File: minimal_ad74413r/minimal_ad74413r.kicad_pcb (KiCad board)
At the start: 4 copper layers, 30.5 x 25.4 mm, 17 parts, among them U8 AD74413RBCPZ

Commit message: backup
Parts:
- added C1: 0.01 uF, capacitor_footprints:C_0402_1005Metric, F.Cu at (161.6, 105.2)
- added C10: 0.01 uF, capacitor_footprints:C_0402_1005Metric, F.Cu at (141.9, 97.0)
- added C11: 220 pF, capacitor_footprints:C_0402_1005Metric, F.Cu at (138.7, 99.2)
- added C12: 0.01 uF, capacitor_footprints:C_0402_1005Metric, F.Cu at (137.9, 97.4)
- added C13: 0.01 uF, capacitor_footprints:C_0402_1005Metric, F.Cu at (141.9, 105.2)
- added C14: 0.01 uF, capacitor_footprints:C_0402_1005Metric, F.Cu at (141.9, 108.5)
- added C15: 220 pF, capacitor_footprints:C_0402_1005Metric, F.Cu at (138.7, 106.3)
- added C16: 0.01 uF, capacitor_footprints:C_0402_1005Metric, F.Cu at (137.9, 108.1)
- added C2: 0.01 uF, capacitor_footprints:C_0402_1005Metric, F.Cu at (161.6, 108.5)
- added C3: 220 pF, capacitor_footprints:C_0402_1005Metric, F.Cu at (164.9, 106.3)
- added C4: 0.01 uF, capacitor_footprints:C_0402_1005Metric, F.Cu at (165.7, 108.1)
- added C5: 0.01 uF, capacitor_footprints:C_0402_1005Metric, F.Cu at (161.6, 100.3)
- added C6: 0.01 uF, capacitor_footprints:C_0402_1005Metric, F.Cu at (161.6, 97.0)
- added C7: 220 pF, capacitor_footprints:C_0402_1005Metric, F.Cu at (164.9, 99.2)
- added C8: 0.01 uF, capacitor_footprints:C_0402_1005Metric, F.Cu at (165.7, 97.4)
- added C9: 0.01 uF, capacitor_footprints:C_0402_1005Metric, F.Cu at (141.9, 100.3)
- added CR1: SBAV99WT1G, diode_footprints:SC_70, F.Cu at (162.4, 112.7)
- added CR2: SBAV99WT1G, diode_footprints:SC_70, F.Cu at (162.4, 92.8)
- added CR3: SBAV99WT1G, diode_footprints:SC_70, F.Cu at (141.1, 92.8)
- added CR4: SBAV99WT1G, diode_footprints:SC_70, F.Cu at (141.1, 112.7)
- added Q1: ZXMP6A17E6TA, transistor_footprints:SOT-26, F.Cu at (159.0, 112.0)
- added Q2: ZXMP6A17E6TA, transistor_footprints:SOT-26, F.Cu at (159.0, 93.5)
- added Q3: ZXMP6A17E6TA, transistor_footprints:SOT-26, F.Cu at (144.5, 93.5)
- added Q4: ZXMP6A17E6TA, transistor_footprints:SOT-26, F.Cu at (144.5, 112.0)
- added R1: 2k, resistor_footprints:R_0402_1005Metric, F.Cu at (161.6, 110.8)
- added R10: 100, resistor_footprints:R_0805_2012Metric, F.Cu at (164.1, 97.0)
- added R11: 2k, resistor_footprints:R_0402_1005Metric, F.Cu at (141.9, 94.7)
- added R12: 10k, resistor_footprints:R_0402_1005Metric, F.Cu at (141.9, 95.9)
- added R13: 2k, resistor_footprints:R_0402_1005Metric, F.Cu at (141.9, 98.1)
- added R14: 10k, resistor_footprints:R_0402_1005Metric, F.Cu at (141.9, 99.2)
- added R15: 100, resistor_footprints:R_0805_2012Metric, F.Cu at (139.5, 97.0)
- added R16: 2k, resistor_footprints:R_0402_1005Metric, F.Cu at (141.9, 110.8)
- added R17: 10k, resistor_footprints:R_0402_1005Metric, F.Cu at (141.9, 109.6)
- added R18: 2k, resistor_footprints:R_0402_1005Metric, F.Cu at (141.9, 107.4)
- added R19: 10k, resistor_footprints:R_0402_1005Metric, F.Cu at (141.9, 106.3)
- added R2: 10k, resistor_footprints:R_0402_1005Metric, F.Cu at (161.6, 109.6)
- added R20: 100, resistor_footprints:R_0805_2012Metric, F.Cu at (139.5, 108.5)
- added R3: 2k, resistor_footprints:R_0402_1005Metric, F.Cu at (161.6, 107.4)
- added R4: 10k, resistor_footprints:R_0402_1005Metric, F.Cu at (161.6, 106.3)
- added R5: 100, resistor_footprints:R_0805_2012Metric, F.Cu at (164.1, 108.5)
- added R6: 2k, resistor_footprints:R_0402_1005Metric, F.Cu at (161.6, 94.7)
- added R7: 10k, resistor_footprints:R_0402_1005Metric, F.Cu at (161.6, 95.9)
- added R8: 2k, resistor_footprints:R_0402_1005Metric, F.Cu at (161.6, 98.1)
- added R9: 10k, resistor_footprints:R_0402_1005Metric, F.Cu at (161.6, 99.2)
- added TP1: TestPoint, test_point_footprints:TestPoint_THTPad_Castelated, F.Cu at (157.5, 118.7)
- added TP10: TestPoint, test_point_footprints:TestPoint_THTPad_Castelated, F.Cu at (149.9, 118.7)
- added TP11: TestPoint, test_point_footprints:TestPoint_THTPad_Castelated, F.Cu at (167.6, 113.7)
- added TP12: TestPoint, test_point_footprints:TestPoint_THTPad_Castelated, F.Cu at (167.6, 92.1)
- added TP13: TestPoint, test_point_footprints:TestPoint_THTPad_Castelated, F.Cu at (135.9, 92.1)
- added TP14: TestPoint, test_point_footprints:TestPoint_THTPad_Castelated, F.Cu at (135.9, 113.7)
- added TP15: TestPoint, test_point_footprints:TestPoint_THTPad_Castelated, F.Cu at (166.4, 113.7)
- added TP16: TestPoint, test_point_footprints:TestPoint_THTPad_Castelated, F.Cu at (166.4, 92.1)
- added TP17: TestPoint, test_point_footprints:TestPoint_THTPad_Castelated, F.Cu at (137.2, 92.1)
- added TP18: TestPoint, test_point_footprints:TestPoint_THTPad_Castelated, F.Cu at (137.2, 113.7)
- added TP19: TestPoint, test_point_footprints:TestPoint_THTPad_Castelated, F.Cu at (154.9, 87.0)
- added TP2: TestPoint, test_point_footprints:TestPoint_THTPad_Castelated, F.Cu at (156.2, 118.7)
- added TP20: TestPoint, test_point_footprints:TestPoint_THTPad_Castelated, F.Cu at (153.7, 87.0)
- added TP21: TestPoint, test_point_footprints:TestPoint_THTPad_Castelated, F.Cu at (152.4, 87.0)
- added TP22: TestPoint, test_point_footprints:TestPoint_THTPad_Castelated, F.Cu at (151.1, 87.0)
- added TP23: TestPoint, test_point_footprints:TestPoint_THTPad_Castelated, F.Cu at (149.9, 87.0)
- added TP24: TestPoint, test_point_footprints:TestPoint_THTPad_Castelated, F.Cu at (148.6, 87.0)
- added TP3: TestPoint, test_point_footprints:TestPoint_THTPad_Castelated, F.Cu at (154.9, 118.7)
- added TP4: TestPoint, test_point_footprints:TestPoint_THTPad_Castelated, F.Cu at (153.7, 118.7)
- added TP5: TestPoint, test_point_footprints:TestPoint_THTPad_Castelated, F.Cu at (152.4, 118.7)
- added TP6: TestPoint, test_point_footprints:TestPoint_THTPad_Castelated, F.Cu at (148.6, 118.7)
- added TP7: TestPoint, test_point_footprints:TestPoint_THTPad_Castelated, F.Cu at (147.3, 118.7)
- added TP8: TestPoint, test_point_footprints:TestPoint_THTPad_Castelated, F.Cu at (146.1, 118.7)
- added TP9: TestPoint, test_point_footprints:TestPoint_THTPad_Castelated, F.Cu at (151.1, 118.7)
- C82: footprint footprints:C_0603_1608Metric -> capacitor_footprints:C_0603_1608Metric
- moved C89 4.29 mm to (155.2, 92.5), turned to 90 degrees
- moved C91 2.89 mm to (149.9, 112.4), turned to 180 degrees
- moved C83 2.36 mm to (152.1, 112.4), turned to 0 degrees
- moved C93 2.22 mm to (142.3, 103.6)
- moved C84 2.06 mm to (152.1, 111.1), turned to 0 degrees
- moved C92 1.98 mm to (138.6, 102.9)
- moved U8 1.65 mm to (151.8, 102.9)
- moved C81 1.65 mm to (149.0, 96.6)
- moved C82 1.65 mm to (151.5, 95.7)
- moved C87 1.65 mm to (159.8, 102.6)
- moved C90 1.50 mm to (153.0, 93.5), turned to 90 degrees
- moved C95 1.46 mm to (165.0, 102.9)
- moved C86 1.43 mm to (162.1, 101.7)
- moved C94 1.43 mm to (162.1, 103.6)
- moved C85 1.43 mm to (163.2, 101.7)
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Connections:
- C88 pad 1: (no net) -> /3V3
- C89 pad 1: /3V3_ISO -> /3V3
- C90 pad 1: /3V3_ISO -> /3V3
- C91 pad 1: (no net) -> /3V3
- U8 pad 23: /3V3_ISO -> /3V3
- U8 pad 28: (no net) -> GNDA
- U8 pad 55: (no net) -> /3V3
- U8 pad 56: (no net) -> /3V3
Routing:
- net /3V3_ISO: track 16.6 -> 0.00 mm, vias 4 -> 0
- net /CCOMP_B: track 0.00 -> 15.7 mm, vias 0 -> 2
- net /CCOMP_C: track 0.00 -> 15.7 mm, vias 0 -> 2
- net /CCOMP_A: track 0.00 -> 15.6 mm, vias 0 -> 2
- net /CCOMP_D: track 0.00 -> 15.5 mm, vias 0 -> 2
- net /VIOUTP_C: track 0.00 -> 11.0 mm, vias 0 -> 2
- net /VIOUTP_A: track 0.00 -> 10.9 mm, vias 0 -> 2
- net /SDO: track 0.00 -> 9.13 mm
- net /~{RESET}: track 0.00 -> 9.13 mm
- net /~{ALERT}: track 0.00 -> 9.01 mm
- net /3V3: track 0.00 -> 8.95 mm, vias 0 -> 4
- net /~{LDAC}: track 0.00 -> 8.89 mm
- net /~{ADC_RDY}: track 0.00 -> 8.81 mm
- net /~{SYNC}: track 0.00 -> 8.81 mm
- net /SCLK: track 0.00 -> 8.71 mm
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- added copper zone on F.Cu, net /3V3
- added copper zone on In1.Cu, net /VDD_24V
- added copper zone on In1.Cu, net GNDA
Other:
- board size 30.5 x 25.4 mm -> 34.3 x 31.8 mm

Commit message: backup
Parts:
- added TP25: TestPoint, test_point_footprints:TestPoint_THTPad_Castelated, F.Cu at (133.3, 102.2)
- added TP26: TestPoint, test_point_footprints:TestPoint_THTPad_Castelated, F.Cu at (170.2, 102.2)
- moved TP23 26.2 mm to (170.2, 103.5), turned to 180 degrees
- moved TP24 22.5 mm to (133.3, 103.5), turned to 0 degrees
- moved TP19 1.80 mm to (153.7, 85.7)
- moved TP20 1.80 mm to (152.4, 85.7)
- moved TP22 1.80 mm to (149.9, 85.7)
- moved TP21 1.80 mm to (151.1, 85.7)
- moved C89 1.50 mm to (153.7, 92.4), turned to 180 degrees
- moved C96 1.48 mm to (148.5, 92.4), turned to 180 degrees
- moved TP1 1.27 mm to (157.5, 120.0)
- moved TP10 1.27 mm to (149.9, 120.0)
- moved TP2 1.27 mm to (156.2, 120.0)
- moved TP3 1.27 mm to (154.9, 120.0)
- moved TP4 1.27 mm to (153.7, 120.0)
- moved TP5 1.27 mm to (152.4, 120.0)
- moved TP6 1.27 mm to (148.6, 120.0)
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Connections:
- TP23 pad 1: /3V3 -> /VDD_24V
- TP24 pad 1: GNDA -> /VDD_24V
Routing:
- net /3V3: track 8.95 -> 0.00 mm, vias 4 -> 5
- net /~{ADC_RDY}: track 8.81 -> 11.9 mm
- net /SDI: track 8.49 -> 11.6 mm
- net GNDA: track 17.9 -> 14.8 mm, vias 76 -> 97
- net /SDO: track 9.13 -> 12.2 mm
- net /SCLK: track 8.71 -> 11.7 mm
- net /~{ALERT}: track 9.01 -> 12.0 mm
- net /~{RESET}: track 9.13 -> 12.2 mm
- net /~{LDAC}: track 8.89 -> 11.9 mm
- net /~{SYNC}: track 8.81 -> 11.8 mm
- net /CCOMP_B: track 15.7 -> 12.8 mm
- net /CCOMP_D: track 15.5 -> 13.0 mm
- net /GPO_D: track 10.9 -> 12.6 mm
- net /GPO_C: track 10.7 -> 12.3 mm
- net /CCOMP_C: track 15.7 -> 17.3 mm
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- added copper zone on B.Cu, net /3V3
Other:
- board size 34.3 x 31.8 mm -> 36.8 x 34.3 mm

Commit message: Backup
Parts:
- added J1: CLP-102-02-G-D-BE, connector_footprints:CLP-102-02-G-D-BE, F.Cu at (168.3, 111.1)
- added J2: CLP-102-02-G-D-BE, connector_footprints:CLP-102-02-G-D-BE, F.Cu at (168.3, 94.6)
- added J3: CLP-102-02-G-D-BE, connector_footprints:CLP-102-02-G-D-BE, F.Cu at (135.3, 94.7)
- added J4: CLP-102-02-G-D-BE, connector_footprints:CLP-102-02-G-D-BE, F.Cu at (135.3, 111.0)
- moved TP12 2.84 mm to (168.9, 89.5)
- moved TP13 2.84 mm to (134.6, 89.5)
- moved TP16 2.84 mm to (167.6, 89.5)
- moved TP17 2.84 mm to (135.9, 89.5)
- moved TP11 2.84 mm to (168.9, 116.2)
- moved TP14 2.84 mm to (134.6, 116.2)
- moved TP15 2.84 mm to (167.6, 116.2)
- moved TP18 2.84 mm to (135.9, 116.2)
- moved TP23 1.27 mm to (171.4, 103.5)
- moved TP24 1.27 mm to (132.1, 103.5)
- moved TP25 1.27 mm to (132.1, 102.2)
- moved TP26 1.27 mm to (171.4, 102.2)
- moved Q2 0.10 mm to (159.0, 93.4)
- moved Q3 0.10 mm to (144.5, 93.4)
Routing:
- net Net-(CR4-Pad3): track 0.00 -> 1.11 mm
- net /VIOUTN_D: track 4.26 -> 5.15 mm, vias 1 -> 2
- net /VIOUTN_C: track 4.35 -> 5.24 mm, vias 1 -> 2
- net /VIOUTN_B: track 4.35 -> 5.24 mm, vias 1 -> 2
- net /VIOUTN_A: track 4.26 -> 5.15 mm, vias 1 -> 2
- added copper zone on F.Cu, net Net-(CR1-Pad1)
- added copper zone on F.Cu, net Net-(CR2-Pad1)
- added copper zone on F.Cu, net Net-(CR3-Pad1)
- added copper zone on F.Cu, net Net-(CR4-Pad1)
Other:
- board size 36.8 x 34.3 mm -> 39.4 x 34.3 mm

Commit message: Backup
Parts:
- added J5: CLP-102-02-G-D-BE, connector_footprints:CLP-102-02-G-D-BE, F.Cu at (169.5, 102.9)
- added J6: CLP-102-02-G-D-BE, connector_footprints:CLP-102-02-G-D-BE, F.Cu at (134.0, 102.9)
- moved TP19 34.9 mm to (160.0, 120.0), turned to 90 degrees
- moved TP20 34.9 mm to (158.8, 120.0), turned to 90 degrees
- moved TP21 34.9 mm to (157.5, 120.0), turned to 90 degrees
- moved TP22 34.9 mm to (156.2, 120.0), turned to 90 degrees
- moved TP23 3.18 mm to (171.4, 106.7)
- moved TP24 3.18 mm to (132.1, 106.7)
- moved TP25 3.17 mm to (132.1, 99.1)
- moved TP26 3.17 mm to (171.4, 99.1)
- moved TP2 2.54 mm to (153.7, 120.0)
- moved TP3 2.54 mm to (152.4, 120.0)
- moved TP7 2.54 mm to (144.8, 120.0)
- moved TP8 2.54 mm to (143.5, 120.0)
- moved TP9 2.54 mm to (148.6, 120.0)
- moved TP1 2.54 mm to (154.9, 120.0)
- moved TP10 2.54 mm to (147.3, 120.0)
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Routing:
- net /GPO_A: track 11.8 -> 30.4 mm
- net /GPO_C: track 12.3 -> 29.9 mm
- net /GPO_B: track 12.0 -> 29.0 mm
- net /GPO_D: track 12.6 -> 28.5 mm
- net /VIOUTN_C: track 5.24 -> 14.4 mm
- net /VIOUTN_A: track 5.15 -> 14.2 mm
- net /VIOUTN_D: track 5.15 -> 12.2 mm
- net /VIOUTN_B: track 5.24 -> 12.2 mm
- net /CCOMP_D: track 13.0 -> 16.4 mm
- net /CCOMP_B: track 12.8 -> 16.2 mm
- net /VIOUTP_B: track 8.64 -> 10.1 mm
- net /VIOUTP_A: track 10.9 -> 12.2 mm
- net /VIOUTP_C: track 11.1 -> 12.4 mm
- net /VIOUTP_D: track 8.54 -> 9.78 mm
- net /SDO: track 12.2 -> 13.3 mm
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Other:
- board size 39.4 x 34.3 mm -> 39.4 x 30.5 mm

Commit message: Minor updates
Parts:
- added J7: CLP-114-02-G-D-BE, connector_footprints:CLP-114-02-G-D-BE, F.Cu at (151.8, 119.1)
- moved TP13 7.62 mm to (143.5, 127.6)
- moved TP14 7.62 mm to (144.8, 127.6)
- moved TP15 7.62 mm to (146.1, 127.6)
- moved TP16 7.62 mm to (147.3, 127.6)
- moved TP17 7.62 mm to (148.6, 127.6)
- moved TP18 7.62 mm to (149.9, 127.6)
- moved TP19 7.62 mm to (151.1, 127.6)
- moved TP20 7.62 mm to (152.4, 127.6)
- moved TP21 7.62 mm to (153.7, 127.6)
- moved TP22 7.62 mm to (154.9, 127.6)
- moved TP23 7.62 mm to (156.2, 127.6)
- moved TP24 7.62 mm to (157.5, 127.6)
- moved TP25 7.62 mm to (158.8, 127.6)
- moved TP26 7.62 mm to (160.0, 127.6)
- renumbered C96 to C1, C11 to C10, C7 to C11, C9 to C12, C5 to C13, C86 to C14, C85 to C15, C87 to C16, C92 to C17, C95 to C18, C93 to C19, C89 to C2, C94 to C20, C13 to C21, C1 to C22, C15 to C23, C3 to C24, C16 to C25, C4 to C26, C14 to C27, C2 to C28, C88 to C29, C90 to C3, C84 to C30, C91 to C31, C83 to C32, C82 to C4, C81 to C5, C10 to C6, C6 to C7, C12 to C8, C8 to C9, CR3 to CR1, CR4 to CR3, CR1 to CR4, J2 to J1, J3 to J2, J6 to J3, J5 to J4, J4 to J5, J1 to J6, Q2 to Q1, Q3 to Q2, Q1 to Q3, R11 to R1, R9 to R10, R19 to R11, R4 to R12, R18 to R13, R3 to R14, R20 to R15, R5 to R16, R2 to R18, R16 to R19, R6 to R2, R1 to R20, R12 to R3, R7 to R4, R15 to R5, R10 to R6, R13 to R7, R14 to R9, TP13 to TP1, TP18 to TP10, TP15 to TP11, TP11 to TP12, TP8 to TP13, TP7 to TP14, TP6 to TP15, TP10 to TP16, TP9 to TP17, TP5 to TP18, TP4 to TP19, TP17 to TP2, TP3 to TP20, TP2 to TP21, TP1 to TP22, TP22 to TP23, TP21 to TP24, TP20 to TP25, TP19 to TP26, TP16 to TP3, TP12 to TP4, TP25 to TP5, TP26 to TP6, TP24 to TP7, TP23 to TP8, TP14 to TP9, U8 to U1
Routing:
- net /GPO_D: track 28.5 -> 36.5 mm, vias 1 -> 2
- net /~{RESET}: track 12.2 -> 20.1 mm
- net /~{SYNC}: track 12.4 -> 20.3 mm
- net /SDI: track 12.6 -> 20.5 mm
- net /~{LDAC}: track 13.0 -> 20.9 mm
- net /SCLK: track 12.9 -> 20.7 mm
- net /GPO_C: track 29.9 -> 37.8 mm, vias 1 -> 2
- net /~{ALERT}: track 12.7 -> 20.5 mm
- net /~{ADC_RDY}: track 13.0 -> 20.9 mm
- net /GPO_B: track 29.0 -> 36.9 mm, vias 1 -> 2
- net /SDO: track 13.3 -> 21.1 mm
- net /GPO_A: track 30.4 -> 38.1 mm, vias 1 -> 2
- net /3V3: track 0.00 -> 4.04 mm, vias 5 -> 7
- net GNDA: track 14.8 -> 18.8 mm, vias 96 -> 85
- net /CCOMP_D: vias 2 -> 3
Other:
- board size 39.4 x 30.5 mm -> 39.4 x 38.1 mm

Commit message: Minor updates
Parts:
- removed J4: CLP-102-02-G-D-BE, connector_footprints:CLP-102-02-G-D-BE
- added J8: CLP-104-02-G-D-BE, connector_footprints:CLP-104-02-G-D-BE, F.Cu at (170.8, 102.9)
- J3: value CLP-102-02-G-D-BE -> CLP-104-02-G-D-BE; footprint connector_footprints:CLP-102-02-G-D-BE -> connector_footprints:CLP-104-02-G-D-BE
- moved TP12 9.44 mm to (175.3, 109.2), turned to 180 degrees
- moved TP9 9.44 mm to (128.3, 109.2), turned to 0 degrees
- moved TP1 9.44 mm to (128.3, 96.5), turned to 0 degrees
- moved TP4 9.44 mm to (175.3, 96.5), turned to 180 degrees
- moved TP10 7.85 mm to (128.3, 114.3), turned to 0 degrees
- moved TP11 7.85 mm to (175.3, 114.3), turned to 180 degrees
- moved TP2 7.85 mm to (128.3, 91.4), turned to 0 degrees
- moved TP3 7.85 mm to (175.3, 91.4), turned to 180 degrees
- moved TP6 3.81 mm to (175.3, 99.1)
- moved TP8 3.81 mm to (175.3, 106.7)
- moved TP5 3.81 mm to (128.3, 99.1)
- moved TP7 3.81 mm to (128.3, 106.7)
- moved J2 2.64 mm to (132.7, 94.0), turned to -90 degrees
- moved J5 2.64 mm to (132.7, 111.8)
- moved J1 2.62 mm to (170.8, 94.0)
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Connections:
- J1 pad 1: GNDA -> /CHANNEL_2
- J1 pad 4: /CHANNEL_2 -> GNDA
- J2 pad 1: /CHANNEL_3 -> GNDA
- J2 pad 4: GNDA -> /CHANNEL_3
- J3 pad 1: /VDD_24V -> GNDA
- J3 pad 4: GNDA -> /VDD_24V
- J5 pad 1: GNDA -> /CHANNEL_4
- J5 pad 4: /CHANNEL_4 -> GNDA
- J6 pad 1: /CHANNEL_1 -> GNDA
- J6 pad 4: GNDA -> /CHANNEL_1
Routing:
- net /3V3: track 4.04 -> 0.00 mm
- net GNDA: track 18.8 -> 14.8 mm, vias 85 -> 95
- net /GPO_D: track 36.5 -> 34.9 mm
- net /GPO_C: track 37.8 -> 36.3 mm
- net /GPO_B: track 36.9 -> 35.6 mm
- net /~{ADC_RDY}: track 20.9 -> 19.7 mm
- net /~{ALERT}: track 20.5 -> 19.4 mm
- net /~{RESET}: track 20.1 -> 19.0 mm
- net /~{SYNC}: track 20.3 -> 19.2 mm
- net Net-(CR4-Pad3): track 1.11 -> 0.00 mm
- net /GPO_A: track 38.1 -> 37.0 mm
- net /SDI: track 20.5 -> 19.9 mm
- net /CCOMP_D: vias 3 -> 2
- net /VDD_24V: vias 0 -> 12
- added copper zone on F.Cu, net /CHANNEL_1
- added copper zone on F.Cu, net /CHANNEL_2
- added copper zone on F.Cu, net /CHANNEL_3
- added copper zone on F.Cu, net /CHANNEL_4
- added copper zone on F.Cu, net Net-(CR1-Pad3)
- added copper zone on F.Cu, net Net-(CR2-Pad3)
- added copper zone on F.Cu, net Net-(CR3-Pad3)
- added copper zone on F.Cu, net Net-(CR4-Pad3)
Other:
- board size 39.4 x 38.1 mm -> 47 x 36.8 mm

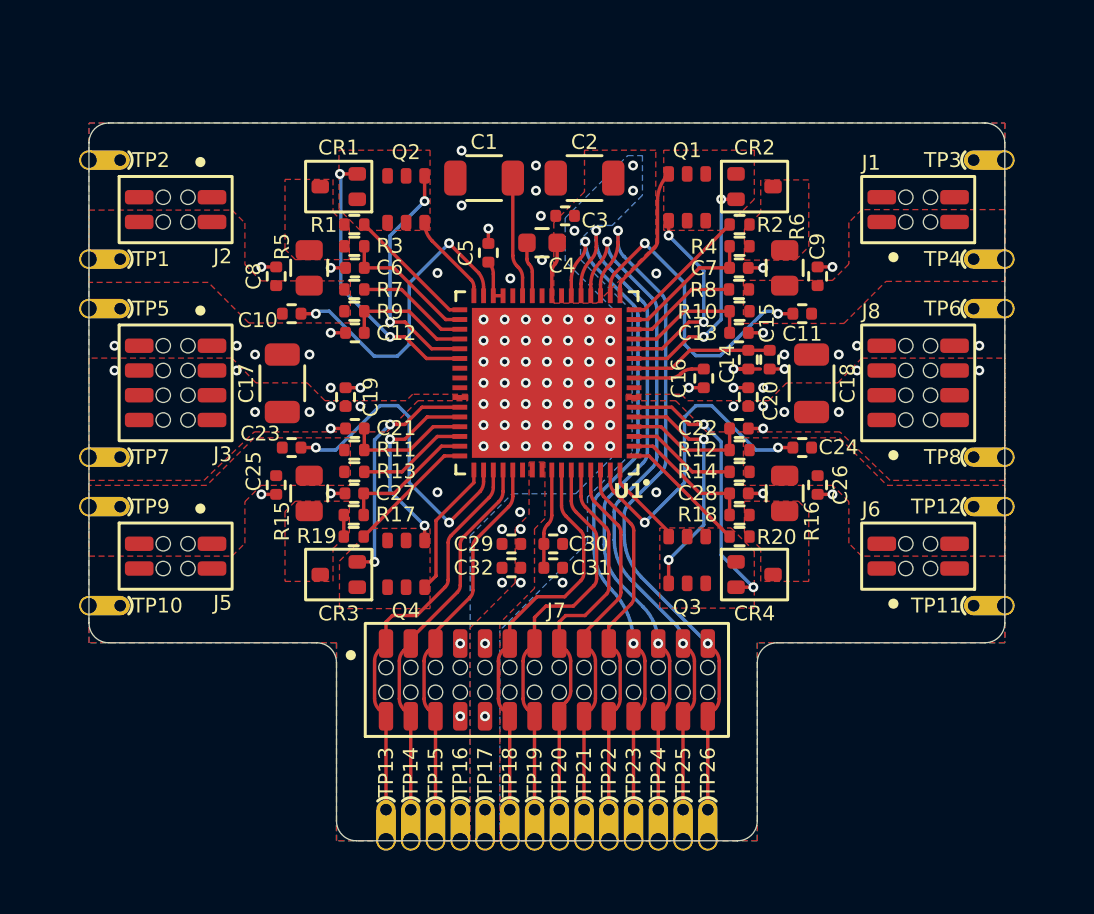
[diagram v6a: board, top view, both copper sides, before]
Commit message: Update references in schematic and update subproject commit
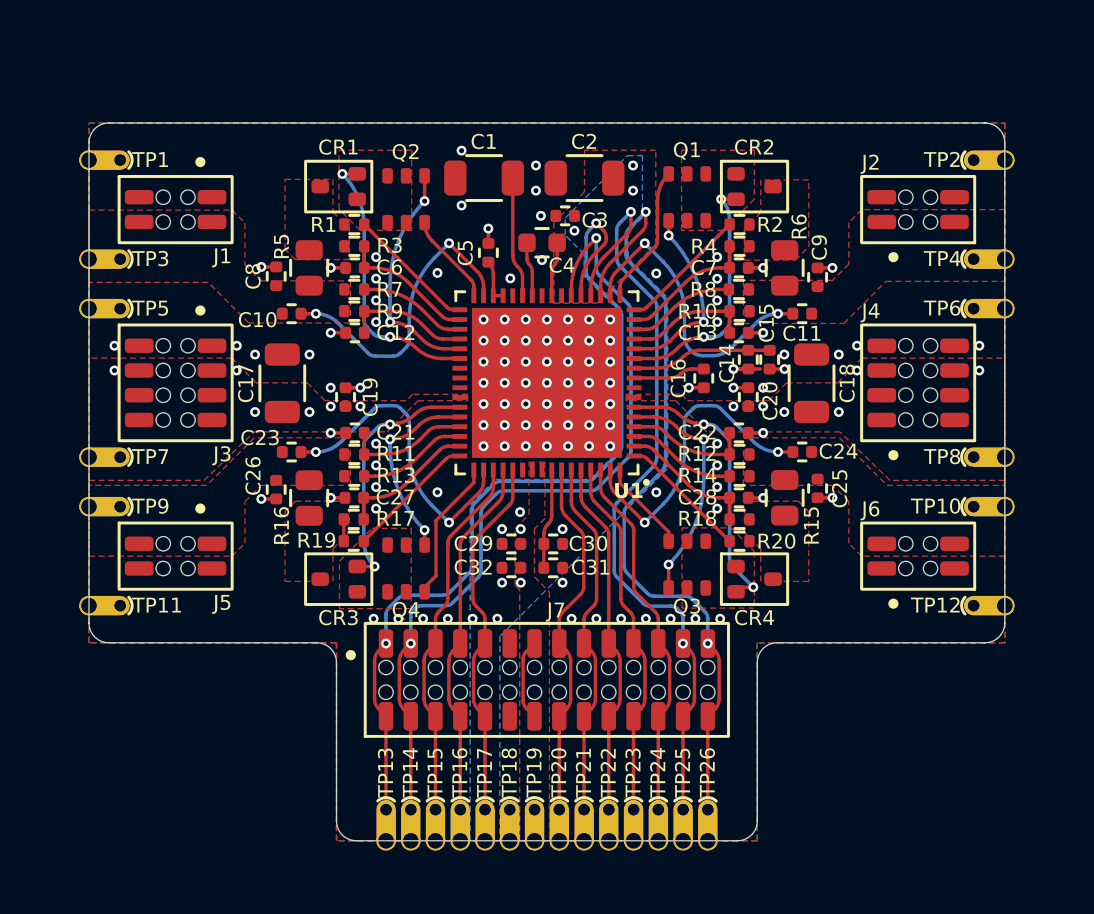
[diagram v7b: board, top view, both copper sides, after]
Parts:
- moved TP13 14.0 mm to (143.5, 126.4)
- moved TP14 11.4 mm to (144.8, 126.4)
- moved TP15 2.54 mm to (146.1, 126.4)
- moved TP16 2.54 mm to (147.3, 126.4)
- moved TP19 2.54 mm to (151.1, 126.4)
- moved TP22 2.54 mm to (154.9, 126.4)
- moved TP23 2.54 mm to (156.2, 126.4)
- moved TP17 2.54 mm to (148.6, 126.4)
- moved TP18 2.54 mm to (149.9, 126.4)
- moved TP20 2.54 mm to (152.4, 126.4)
- moved TP21 2.54 mm to (153.7, 126.4)
- moved TP24 2.54 mm to (157.5, 126.4)
- moved C26 0.24 mm to (137.9, 108.3)
- moved CR3 0.24 mm to (141.1, 112.9)
- moved CR4 0.24 mm to (162.4, 112.9)
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- renumbered C26 to C25, C25 to C26, J2 to J1, J1 to J2, J8 to J4, R16 to R15, R15 to R16, TP2 to TP1, TP12 to TP10, TP10 to TP11, TP11 to TP12, TP24 to TP13, TP23 to TP14, TP13 to TP15, TP14 to TP16, TP15 to TP17, TP16 to TP18, TP17 to TP19, TP3 to TP2, TP18 to TP20, TP19 to TP21, TP20 to TP22, TP21 to TP23, TP22 to TP24, TP1 to TP3
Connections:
- J7 pad 1: /SDO -> /GPO_C
- J7 pad 10: /3V3 -> /~{ALERT}
- J7 pad 11: /~{LDAC} -> GNDA
- J7 pad 12: /~{LDAC} -> GNDA
- J7 pad 13: /SCLK -> /3V3
- J7 pad 14: /SCLK -> /3V3
- J7 pad 15: /SDI -> /~{LDAC}
- J7 pad 16: /SDI -> /~{LDAC}
- J7 pad 17: /~{SYNC} -> /SCLK
- J7 pad 18: /~{SYNC} -> /SCLK
- J7 pad 19: /~{RESET} -> /SDI
- J7 pad 2: /SDO -> /GPO_C
- J7 pad 20: /~{RESET} -> /SDI
- J7 pad 21: /GPO_D -> /~{SYNC}
- J7 pad 22: /GPO_D -> /~{SYNC}
- J7 pad 23: /GPO_C -> /~{RESET}
- J7 pad 24: /GPO_C -> /~{RESET}
- J7 pad 3: /~{ADC_RDY} -> /GPO_D
- J7 pad 4: /~{ADC_RDY} -> /GPO_D
- J7 pad 5: /~{ALERT} -> /SDO
- J7 pad 6: /~{ALERT} -> /SDO
- J7 pad 7: GNDA -> /~{ADC_RDY}
- J7 pad 8: GNDA -> /~{ADC_RDY}
- J7 pad 9: /3V3 -> /~{ALERT}
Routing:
- net /GPO_C: track 36.3 -> 44.7 mm
- net /GPO_D: track 34.9 -> 42.1 mm
- net /GPO_B: track 35.6 -> 40.1 mm
- net /3V3: track 0.00 -> 4.17 mm, vias 7 -> 5
- net /GPO_A: track 37.0 -> 41.0 mm
- net /~{LDAC}: track 20.6 -> 18.7 mm
- net /SCLK: track 20.4 -> 18.5 mm
- net /SDO: track 20.8 -> 19.0 mm
- net /SDI: track 19.9 -> 18.4 mm
- net /~{ADC_RDY}: track 19.7 -> 18.7 mm
- net /VIOUTN_D: track 12.2 -> 12.9 mm
- net /~{ALERT}: track 19.4 -> 18.8 mm
- net /~{SYNC}: track 19.2 -> 18.6 mm
- net /VIOUTN_B: track 12.2 -> 12.7 mm
- net GNDA: vias 95 -> 122

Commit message: Minor updates to project files
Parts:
- moved TP7 7.24 mm to (134.0, 102.2)
- moved TP8 7.24 mm to (169.5, 102.2)
- moved TP13 6.98 mm to (143.5, 119.4)
- moved TP14 6.98 mm to (144.8, 119.4)
- moved TP15 6.98 mm to (146.1, 119.4)
- moved TP16 6.98 mm to (147.3, 119.4)
- moved TP17 6.98 mm to (148.6, 119.4)
- moved TP18 6.98 mm to (149.9, 119.4)
- moved TP19 6.98 mm to (151.1, 119.4)
- moved TP20 6.98 mm to (152.4, 119.4)
- moved TP21 6.98 mm to (153.7, 119.4)
- moved TP22 6.98 mm to (154.9, 119.4)
- moved TP23 6.98 mm to (156.2, 119.4)
- moved TP24 6.98 mm to (157.5, 119.4)
- moved TP25 6.98 mm to (158.8, 119.4)
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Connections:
- J7 pad 10: /~{ALERT} -> GNDA
- J7 pad 14: /3V3 -> GNDA
- J7 pad 16: /~{LDAC} -> GNDA
- J7 pad 18: /SCLK -> GNDA
- J7 pad 2: /GPO_C -> GNDA
- J7 pad 20: /SDI -> GNDA
- J7 pad 22: /~{SYNC} -> GNDA
- J7 pad 24: /~{RESET} -> GNDA
- J7 pad 26: /GPO_B -> GNDA
- J7 pad 28: /GPO_A -> GNDA
- J7 pad 4: /GPO_D -> GNDA
- J7 pad 6: /SDO -> GNDA
- J7 pad 8: /~{ADC_RDY} -> GNDA
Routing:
- net /GPO_D: track 42.1 -> 36.5 mm, vias 2 -> 1
- net /SDO: track 19.0 -> 13.5 mm
- net /~{ADC_RDY}: track 18.7 -> 13.2 mm
- net /~{ALERT}: track 18.8 -> 13.4 mm
- net /~{LDAC}: track 18.7 -> 13.3 mm
- net /SCLK: track 18.5 -> 13.1 mm
- net /SDI: track 18.4 -> 12.9 mm
- net /GPO_A: track 41.0 -> 35.5 mm, vias 2 -> 1
- net /~{SYNC}: track 18.6 -> 13.2 mm
- net /~{RESET}: track 19.0 -> 13.5 mm
- net /GPO_B: track 40.1 -> 34.7 mm, vias 2 -> 1
- net /GPO_C: track 44.7 -> 39.3 mm, vias 2 -> 1
- net /3V3: track 4.17 -> 0.00 mm, vias 5 -> 6
- net GNDA: vias 122 -> 117
- net /VDD_24V: vias 12 -> 8
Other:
- board size 47 x 36.8 mm -> 52.1 x 37.5 mm
